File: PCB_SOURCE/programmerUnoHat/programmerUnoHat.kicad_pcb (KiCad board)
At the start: 2 copper layers, 20 x 51 mm, 5 parts, among them J101 Conn_01x06_Pin

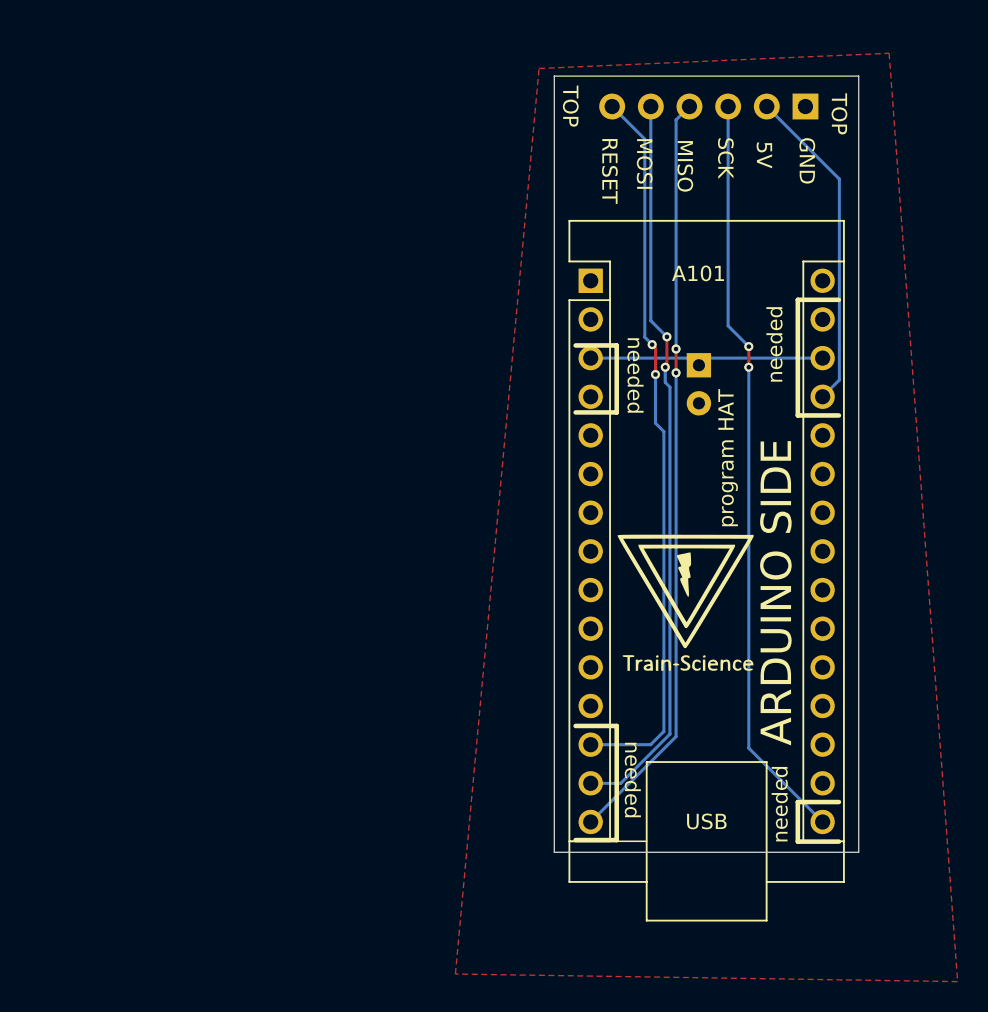
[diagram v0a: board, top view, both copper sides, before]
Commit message: added S88 current sense to releases and update OSSD decoder
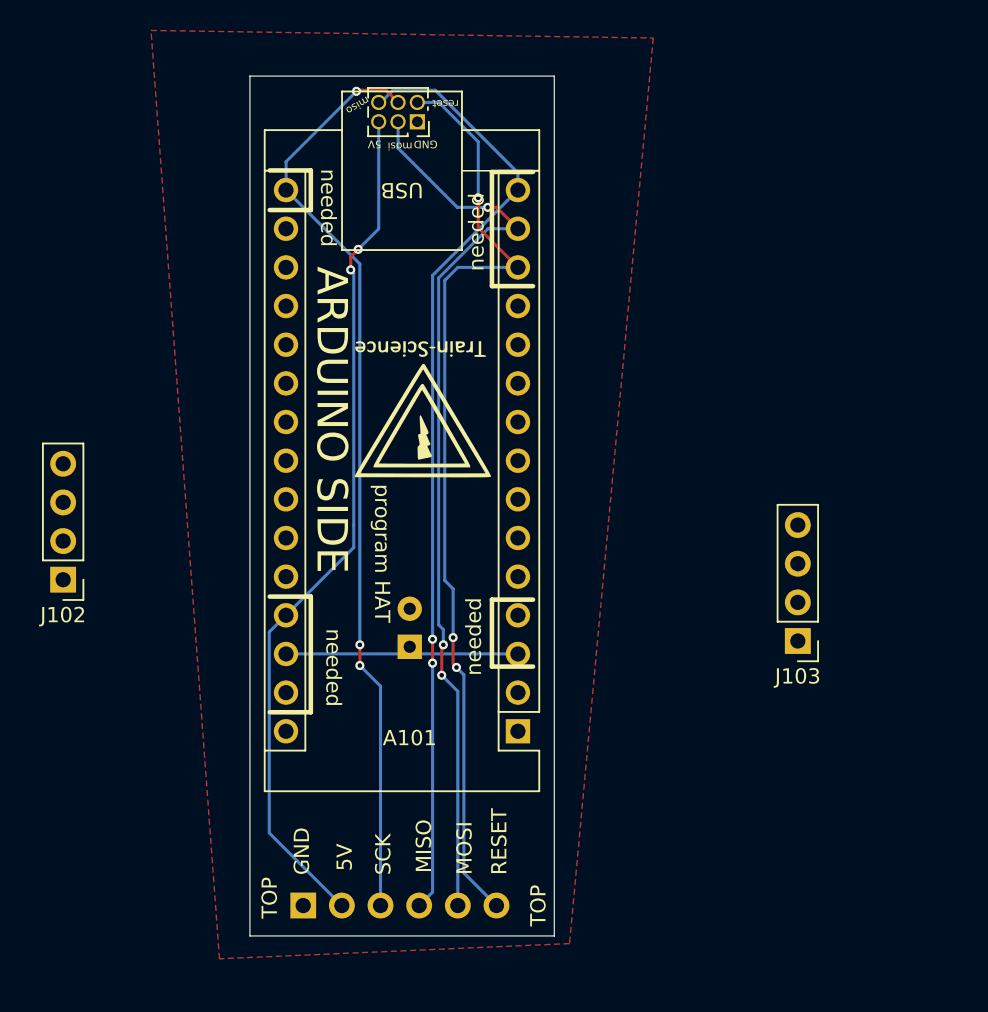
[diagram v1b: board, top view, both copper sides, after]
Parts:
- added J102: Conn_01x04_Pin, Connector_PinHeader_2.54mm:PinHeader_1x04_P2.54mm_Vertical, F.Cu at (91.7, 96.1)
- added J103: Conn_01x04_Pin, Connector_PinHeader_2.54mm:PinHeader_1x04_P2.54mm_Vertical, F.Cu at (140.0, 100.1)
- added U101: HEADER_3x2, Connector_PinSocket_1.27mm:PinSocket_2x03_P1.27mm_Vertical, F.Cu at (115.0, 66.0)
- moved J101 62.0 mm to (107.5, 117.5), turned to -90 degrees
- moved A101 30.0 mm to (121.6, 106.0), turned to 180 degrees
- moved G*** 27.4 mm to (115.4, 80.6), turned to 0 degrees
- moved C101 26.5 mm to (114.5, 100.5), turned to 90 degrees
- moved G*** 21.7 mm to (115.3, 84.8), turned to 180 degrees
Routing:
- net +5V: track 21.5 -> 56.6 mm, vias 0 -> 2
- net /RESET_SLAVE: track 47.6 -> 62.1 mm, vias 2 -> 3
- net /MISO: track 49.7 -> 62.6 mm
- net /MOSI: track 48.4 -> 60.2 mm, vias 2 -> 3
- net /SCK: track 49.6 -> 61.1 mm, vias 2 -> 3
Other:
- board size 20 x 51 mm -> 20 x 56.5 mm
- board text added: "miso"
- board text added: "mosi"
- board text added: "reset"
